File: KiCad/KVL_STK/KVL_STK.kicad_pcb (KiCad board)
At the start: 4 copper layers, 222.4 x 77.5 mm, 235 parts, among them J1 AudioJack2_Ground, J2 Conn_01x04, J3 AudioJack2_Ground, J4 Conn_01x08, SW1 SW_MEC_5G, SW10 SW_MEC_5G, SW14 SW_MEC_5G, SW15 SW_MEC_5G, SW16 SW_MEC_5G, SW17 SW_MEC_5G, SW18 SW_MEC_5G, SW19 SW_MEC_5G, SW2 SW_MEC_5G, SW20 SW_MEC_5G, SW21 SW_MEC_5G, SW22 SW_MEC_5G, SW23 SW_MEC_5G, SW27 SW_MEC_5G, SW28 SW_MEC_5G, SW29 SW_MEC_5G, SW3 SW_MEC_5G, SW30 SW_MEC_5G, SW31 SW_MEC_5G, SW32 SW_MEC_5G, SW33 SW_MEC_5G, SW34 SW_MEC_5G, SW35 SW_MEC_5G, SW36 SW_MEC_5G, SW4 SW_MEC_5G, SW41 SW_MEC_5G, SW42 SW_MEC_5G, SW44 SW_MEC_5G, SW46 SW_MEC_5G, SW47 SW_MEC_5G, SW48 SW_MEC_5G, SW49 SW_MEC_5G, SW5 SW_MEC_5G, SW6 SW_MEC_5G, SW7 SW_MEC_5G, SW8 SW_MEC_5G, SW9 SW_MEC_5G, U1 74HC164, U2 74HC165, U3 74HC165, U5 ADAU1761BCPZ, U6 MIC2005A-1YM5-TR

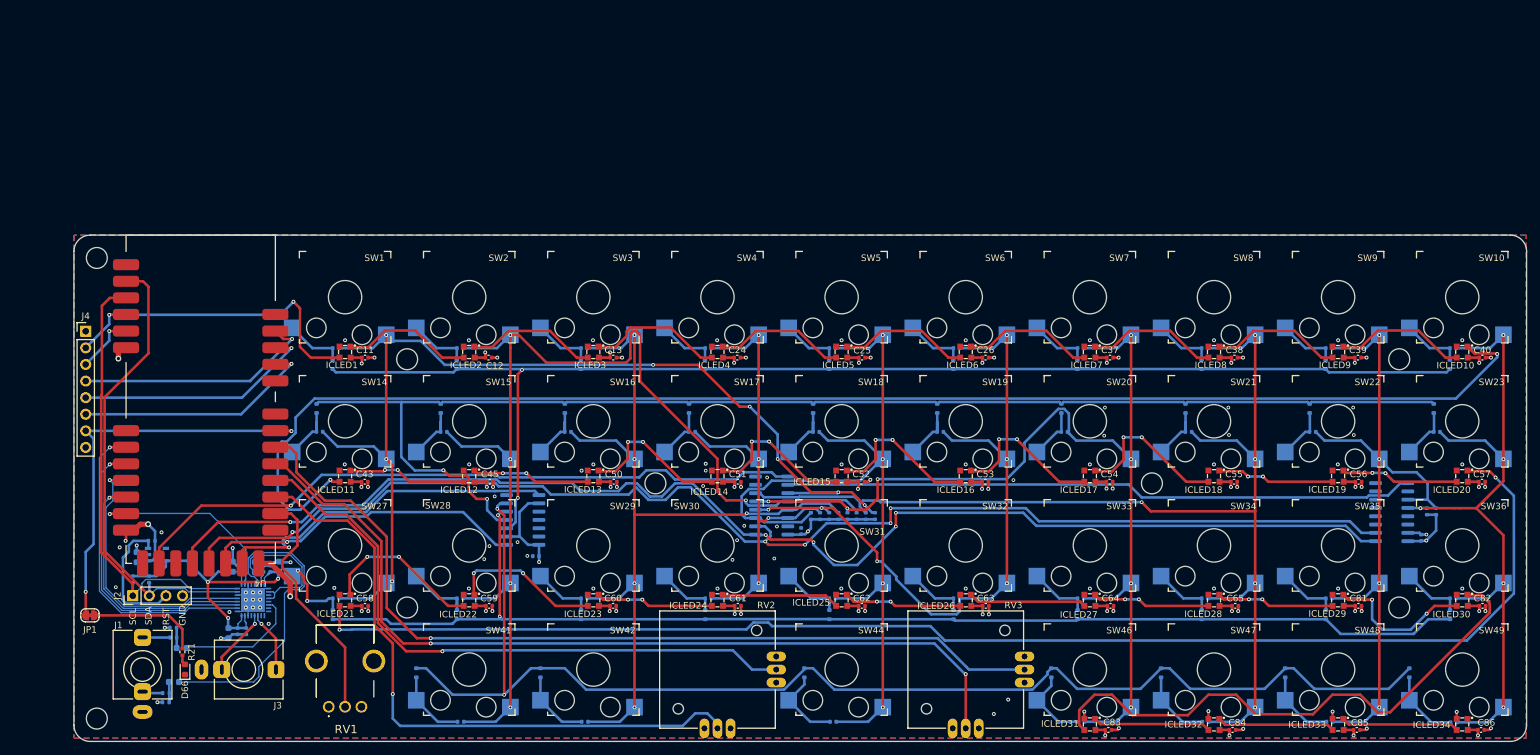
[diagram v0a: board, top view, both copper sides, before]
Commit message: Added STK's schematic & board pdf.
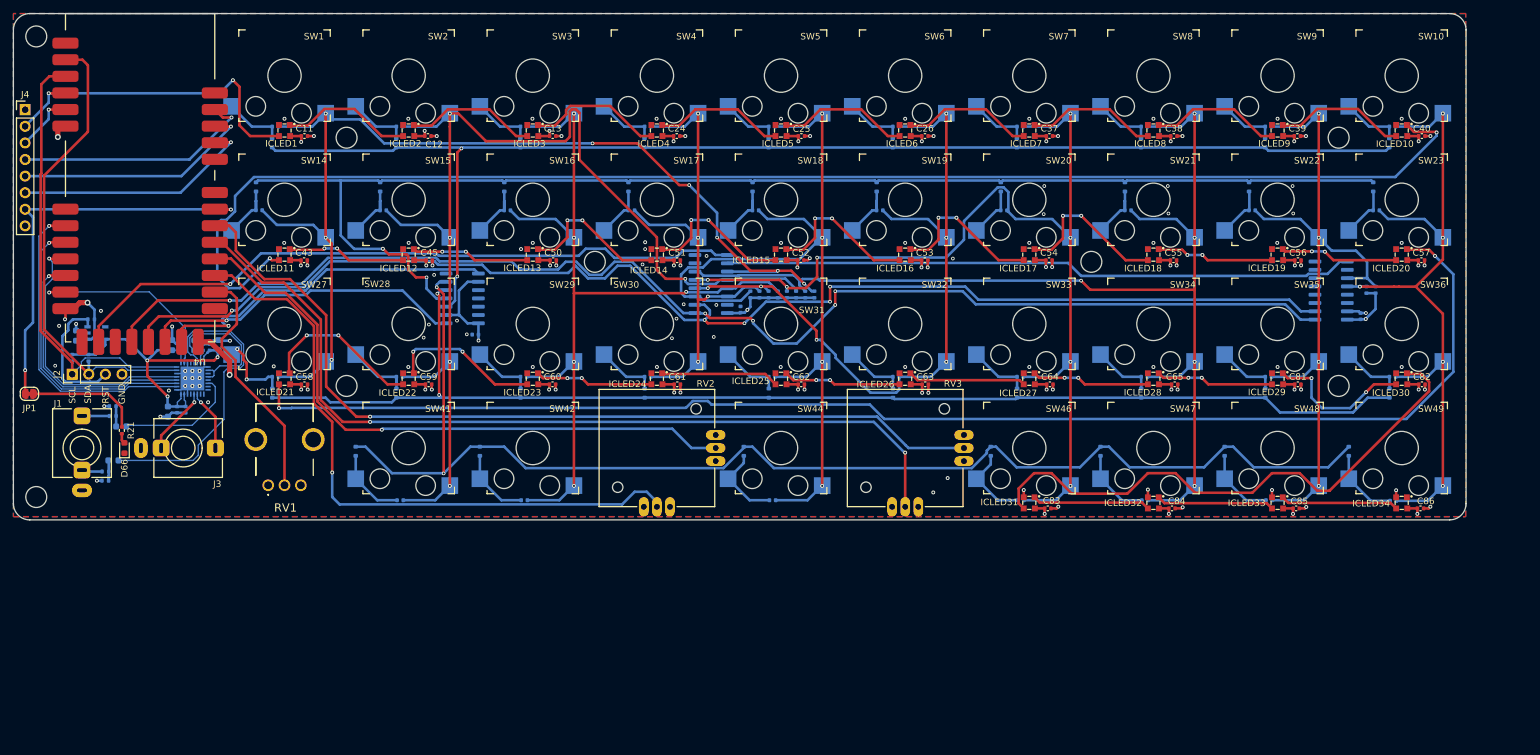
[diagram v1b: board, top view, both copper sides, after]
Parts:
- moved C23 35.2 mm to (257.8, 86.7)
- moved C49 35.2 mm to (260.4, 131.2)
- moved C67 35.2 mm to (160.5, 101.9)
- moved ICLED13 35.2 mm to (128.7, 93.5)
- moved ICLED14 35.2 mm to (147.7, 93.5)
- moved ICLED15 35.2 mm to (166.7, 93.5)
- moved ICLED16 35.2 mm to (185.7, 93.5)
- moved ICLED17 35.2 mm to (204.7, 93.5)
- moved ICLED18 35.2 mm to (223.7, 93.5)
- moved ICLED19 35.2 mm to (242.7, 93.5)
- moved ICLED23 35.2 mm to (128.7, 112.5)
- moved ICLED24 35.2 mm to (147.7, 112.5)
- moved ICLED25 35.2 mm to (166.7, 112.5)
- moved ICLED26 35.2 mm to (185.7, 112.5)
- moved ICLED27 35.2 mm to (204.7, 112.5)
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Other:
- board size 222.4 x 77.5 mm -> 222.3 x 77.5 mm

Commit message: Adjust the position of LEDs on the PCB.
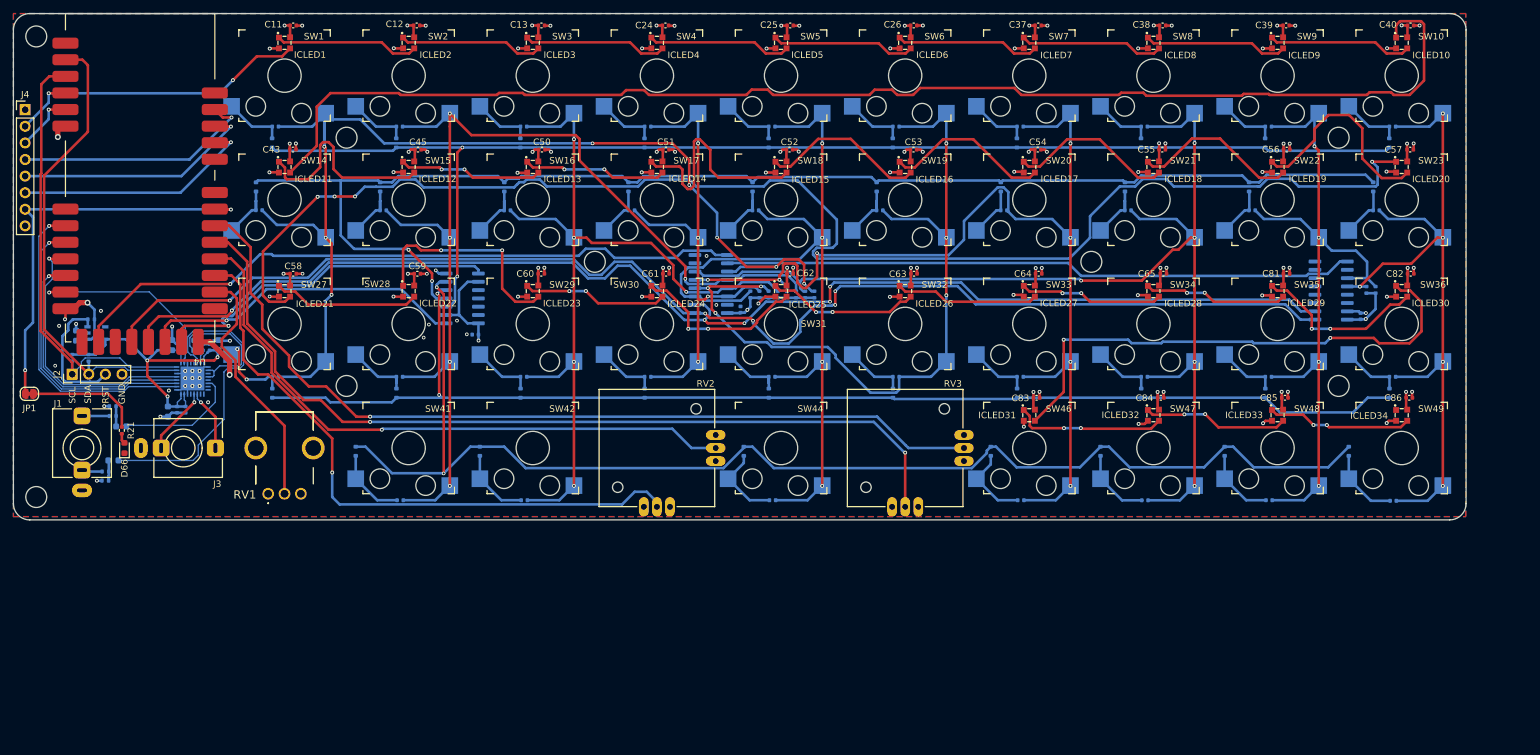
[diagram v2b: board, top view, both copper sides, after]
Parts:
- moved C12 17.0 mm to (111.0, 58.4)
- moved C38 17.0 mm to (225.1, 58.4)
- moved C40 17.0 mm to (263.1, 58.4)
- moved C57 17.0 mm to (263.0, 77.4)
- moved C86 17.0 mm to (262.9, 115.4)
- moved C11 17.0 mm to (92.1, 58.4)
- moved C13 17.0 mm to (130.1, 58.4)
- moved C24 17.0 mm to (149.0, 58.4)
- moved C25 17.0 mm to (168.1, 58.4)
- moved C26 17.0 mm to (187.0, 58.4)
- moved C37 17.0 mm to (206.1, 58.4)
- moved C39 17.0 mm to (244.0, 58.4)
- moved C43 17.0 mm to (92.0, 77.4)
- moved C45 17.0 mm to (111.2, 77.4)
- moved C50 17.0 mm to (130.1, 77.4)
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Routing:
- net GND: track 70.2 -> 120.1 mm, vias 112 -> 96
- net Net-(ICLED10-DOUT): track 219.5 -> 202.3 mm, vias 2 -> 0
- net Net-(ICLED19-DOUT): track 18.1 -> 32.3 mm, vias 2 -> 0
- net Net-(ICLED11-DOUT): track 18.2 -> 31.6 mm, vias 2 -> 0
- net Net-(ICLED14-DOUT): track 23.4 -> 35.4 mm, vias 2 -> 0
- net Net-(ICLED22-DOUT): track 23.3 -> 33.8 mm
- net Q1: track 174.9 -> 165.5 mm
- net Net-(ICLED24-DOUT): track 18.1 -> 27.1 mm, vias 0 -> 2
- net Net-(ICLED20-DOUT): track 211.8 -> 220.2 mm, vias 2 -> 4
- net Q0: track 163.0 -> 171.3 mm
- net Net-(ICLED18-DOUT): track 18.1 -> 25.6 mm, vias 2 -> 0
- net VCC: track 152.9 -> 159.6 mm
- net Q5: track 110.8 -> 117.3 mm
- net Q6: track 158.4 -> 164.1 mm
- net Net-(ICLED31-DOUT): track 18.1 -> 23.3 mm, vias 0 -> 2
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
